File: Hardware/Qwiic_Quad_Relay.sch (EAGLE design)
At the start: 65 parts, among them J2 Qwiic Right Angle, J3 Qwiic Right Angle, J4 AVR_SPI_PROG_3X2TESTPOINTS, J9 POWER_JACK, K1 RELAY-SPDT-JZC-11F, K2 RELAY-SPDT-JZC-11F, K3 RELAY-SPDT-JZC-11F, K4 RELAY-SPDT-JZC-11F, Q1 600mA/40V, Q2 600mA/40V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

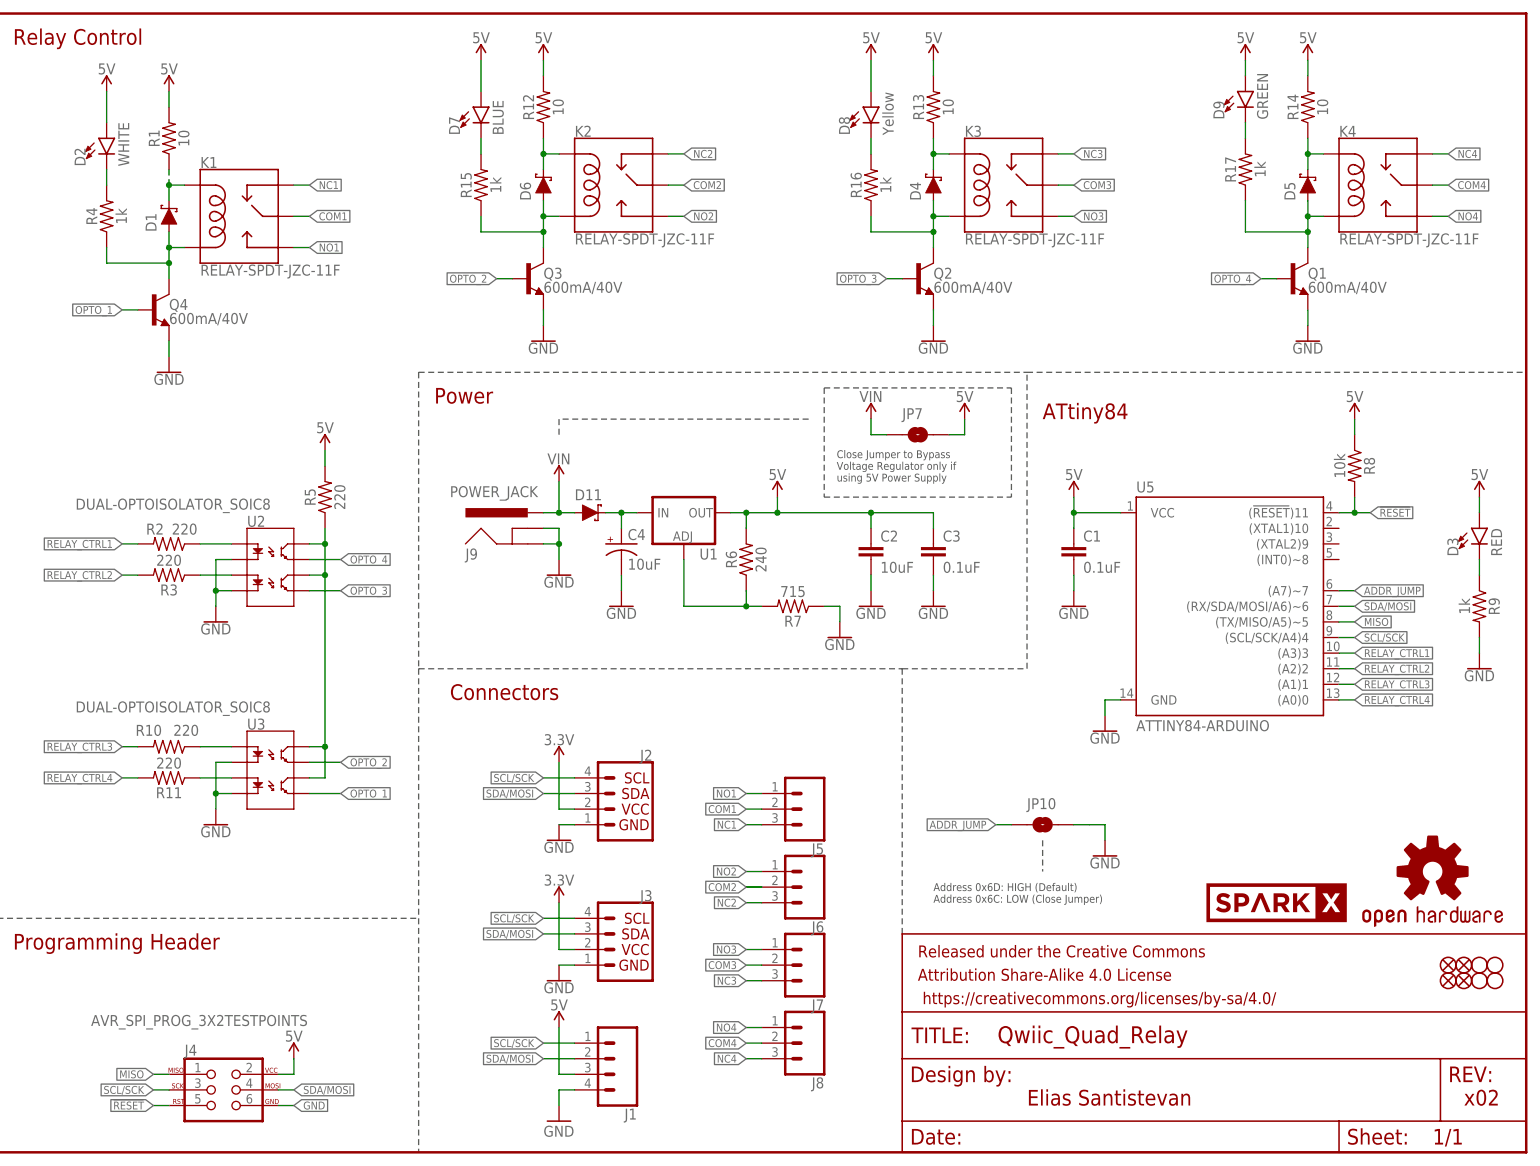
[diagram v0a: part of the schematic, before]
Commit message: Updated to v10 and updated example code that adds commented out line for second i2c address
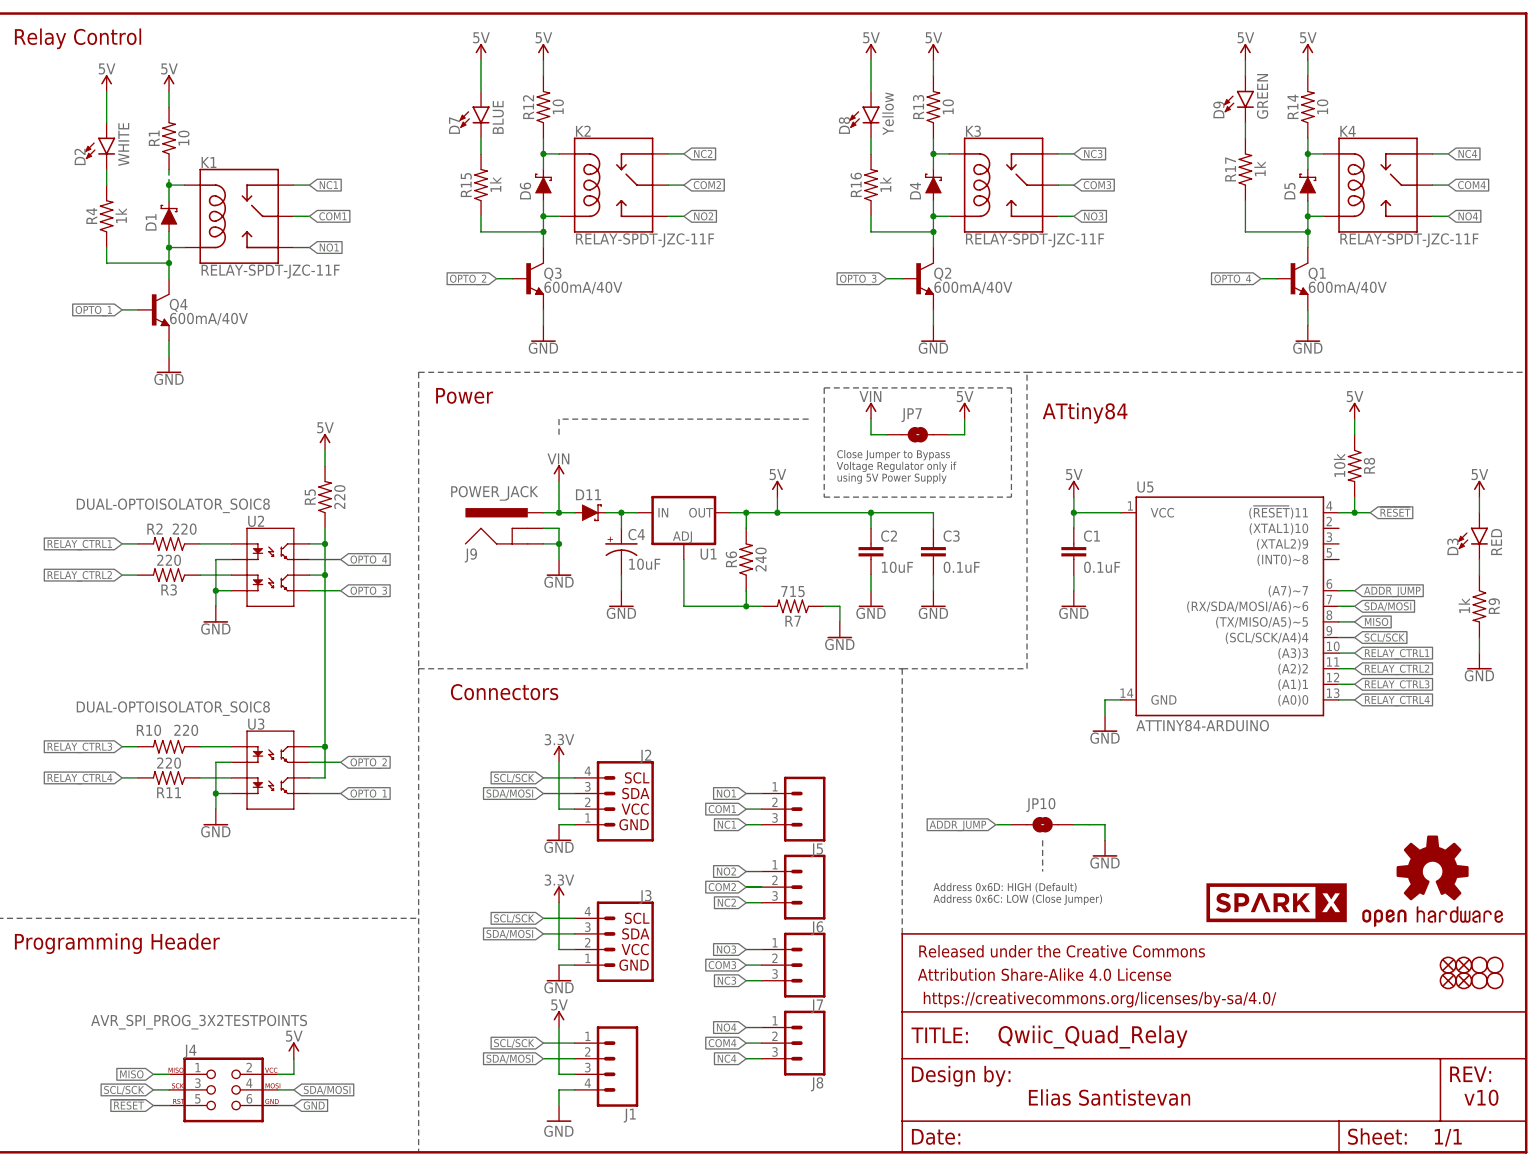
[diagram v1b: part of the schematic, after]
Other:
- note added: "v10"
- note removed: "x02"

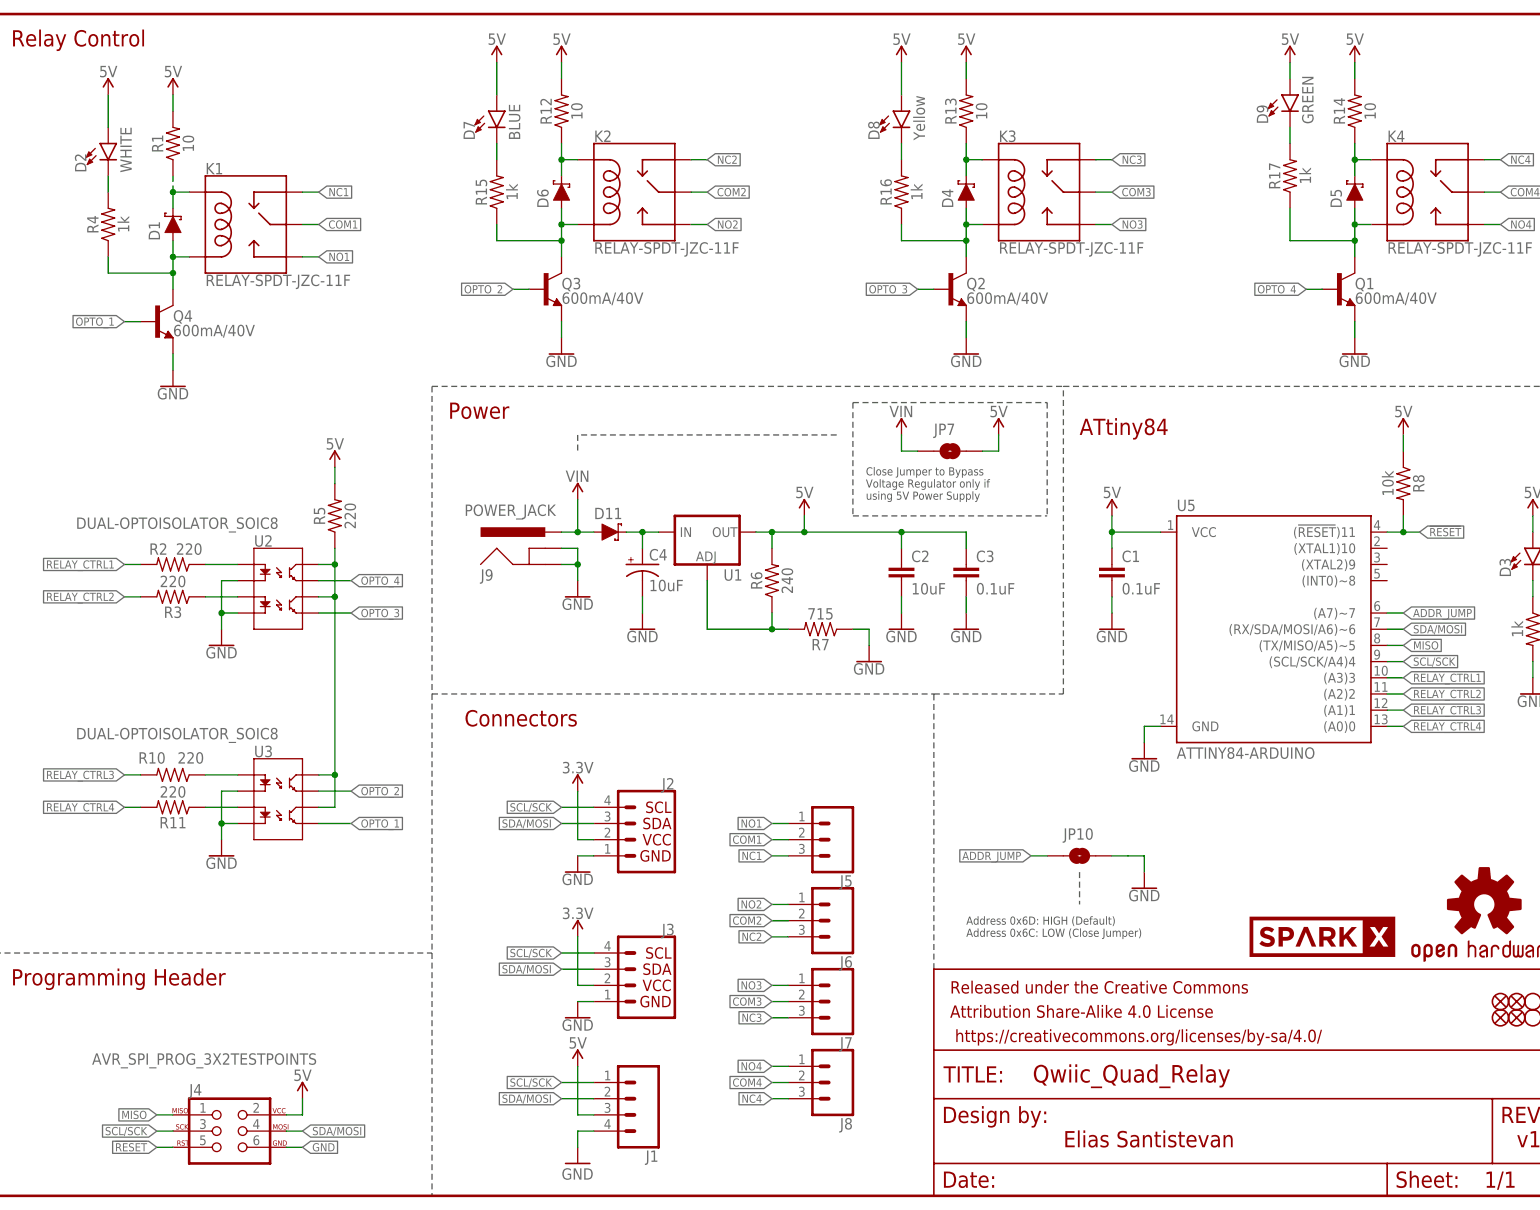
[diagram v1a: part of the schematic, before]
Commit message: Reduces current consumption on every relay channel, seperates 3.3V and 5V system
*Current consumption:
-10 Ohm coil resistor changed to 33 Ohm
-220 Ohm reistor into base of NPN changed to 330
*3.3V Qwiic System:
-Put ATtiny84 back onto the 3.3V Qwiic System
-Changed OptoIsolator resistors from 220 Ohm to 100 Ohm to hit current requirements
*Changed all LEDs to blue
*Changed SparkX labels to SparkFun labels
*Reduced relay trace width to 110 mils (from 160 -overkill)
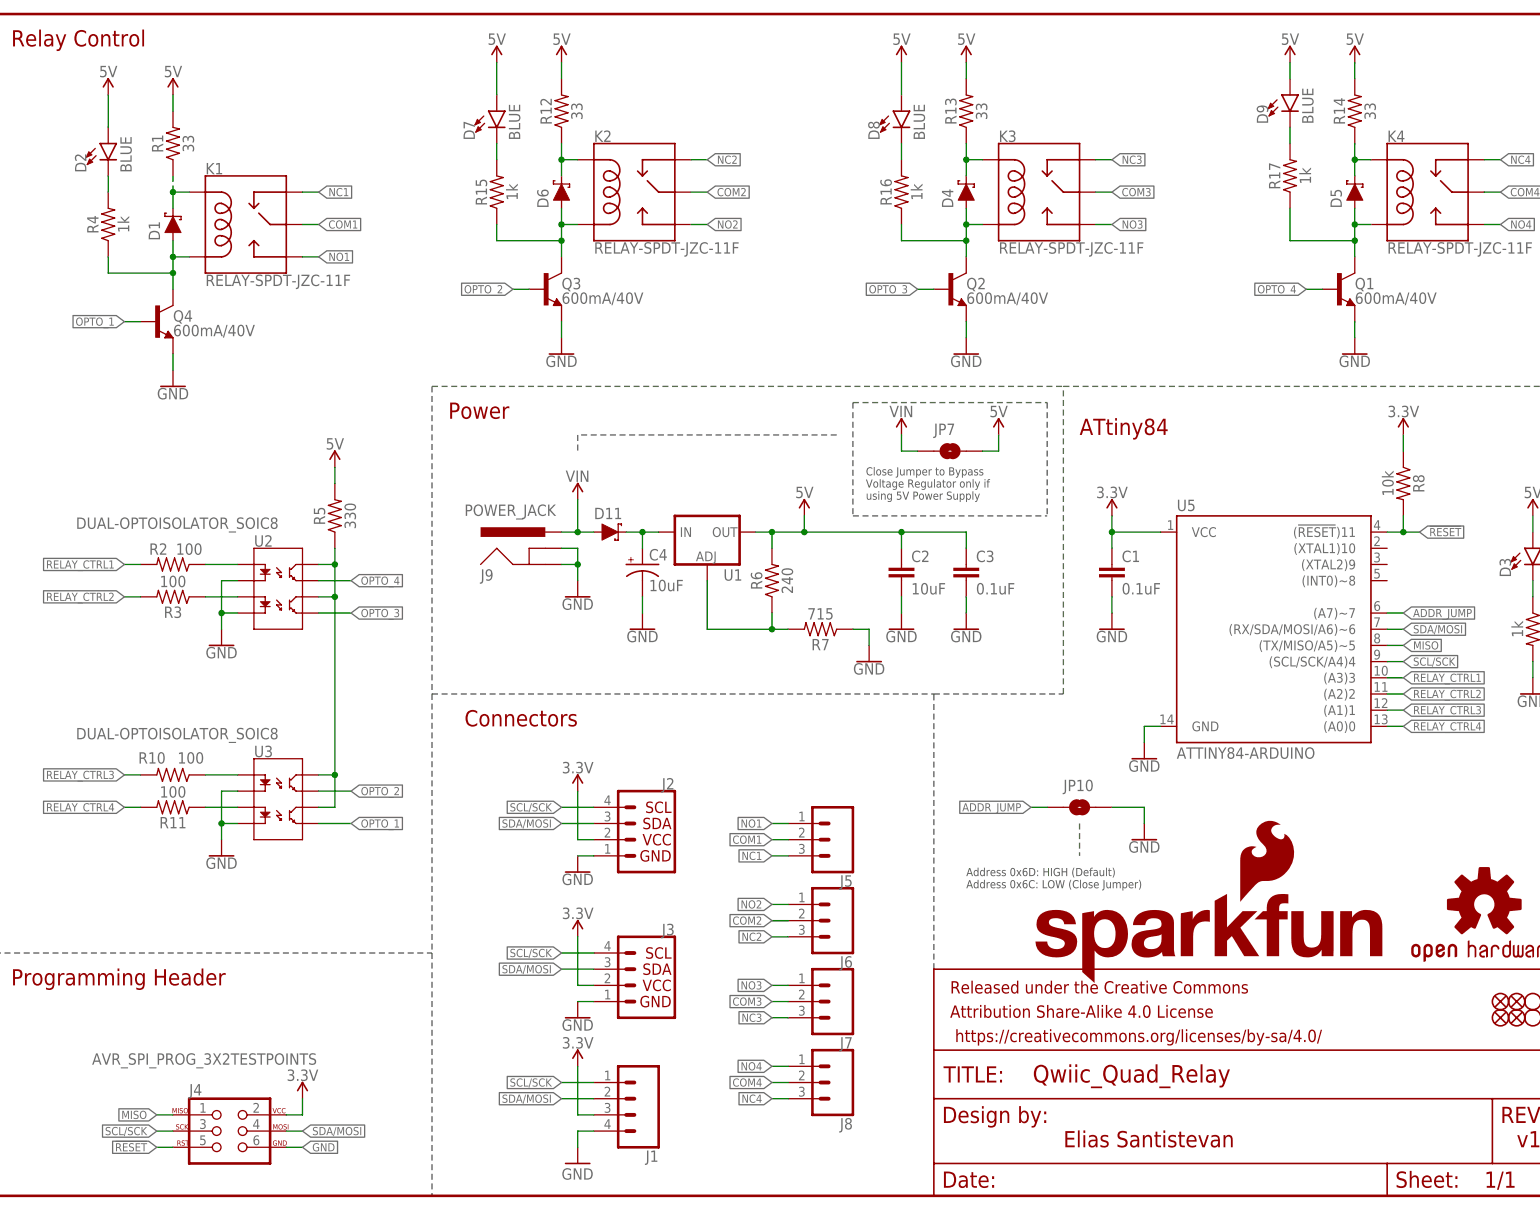
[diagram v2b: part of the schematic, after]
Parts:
- removed U$12: SPARKX-LOGO4, SparkX:SPARKX-LOGO4
- added LOGO2: SFE_LOGO_NAME_FLAME.1_INCH, SparkFun-Aesthetics:SFE_LOGO_NAME_FLAME.1_INCH
- D2: value WHITE -> BLUE; device SparkFun-LED:LED-WHITE0603 -> SparkFun-LED:LED-BLUE0603
- D8: value Yellow -> BLUE; device SparkFun-LED:LED-YELLOW0603 -> SparkFun-LED:LED-BLUE0603
- D9: value GREEN -> BLUE; device SparkFun-LED:LED-GREEN0603 -> SparkFun-LED:LED-BLUE0603
- R1, R12, R13, R14: value 10 -> 33; device SparkFun-Resistors:10OHM-0603-1/10W-5% -> SparkFun-Resistors:33OHM-0603-1/10W-1%
- R10, R11, R2, R3: value 220 -> 100; device SparkFun-Resistors:220OHM-0603-1/10W-1% -> SparkFun-Resistors:100OHM-0603-1/10W-1%
- R5: value 220 -> 330; device SparkFun-Resistors:220OHM-0603-1/10W-1% -> SparkFun-Resistors:330OHM-0603-1/10W-1%
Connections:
- net 3.3V: now also C1.1, J1.3, J4.2, R8.1, U5.VCC
- net 5V: no longer C1.1, J1.3, J4.2, R8.1, U5.VCC
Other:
- moved on the sheet: JP10

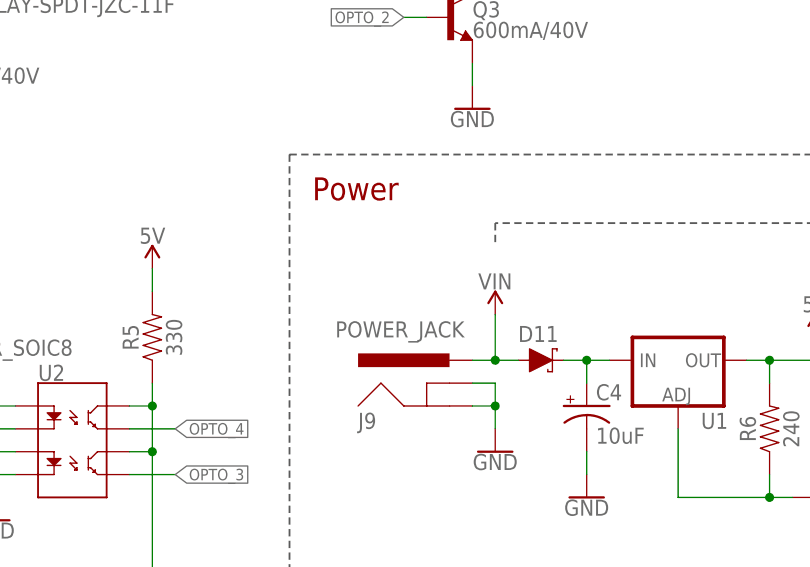
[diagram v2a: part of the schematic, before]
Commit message: Adds selective soldering path to documents layer
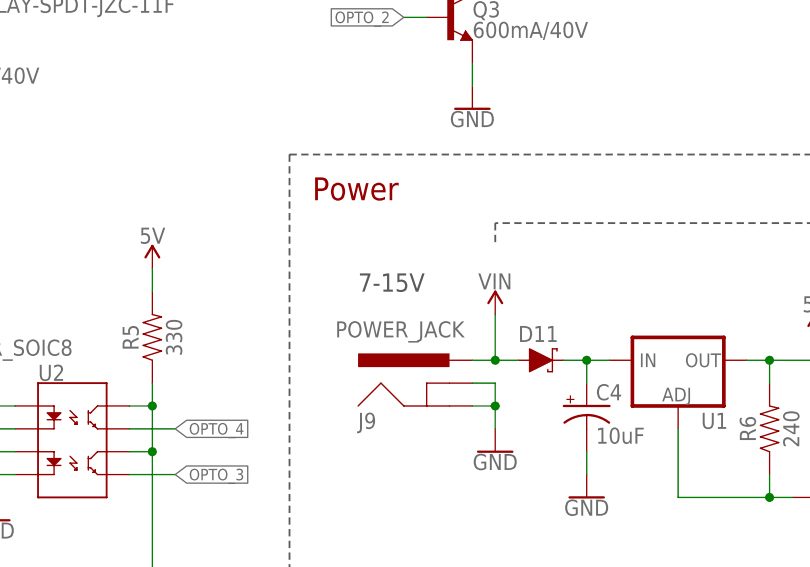
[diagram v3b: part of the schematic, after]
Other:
- note added: "7-15V"
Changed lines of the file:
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@@
 Address 0x6C: LOW (Close Jumper)</text>
 <wire x1="170.18" y1="58.42" x2="170.18" y2="53.34" width="0.2032" layer="97" style="dashdot"/>
+<text x="76.2" y="111.76" size="2.032" layer="97" font="vector">7-15V</text>
 </plain>
 <instances>

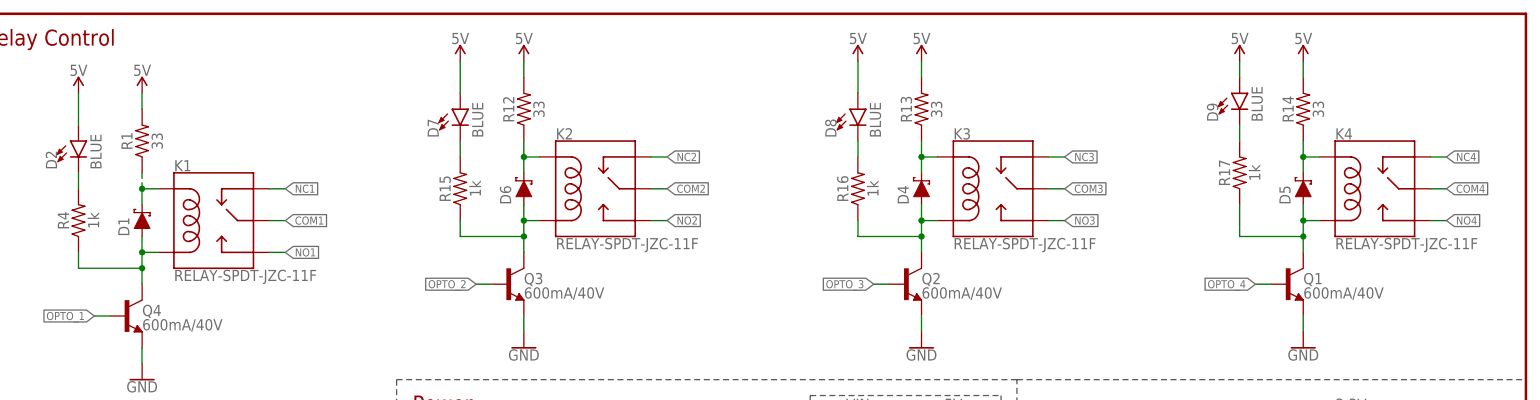
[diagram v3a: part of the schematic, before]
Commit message: Moves 33 Ohm resistor to after the coil so that drop doesn't occur before it.
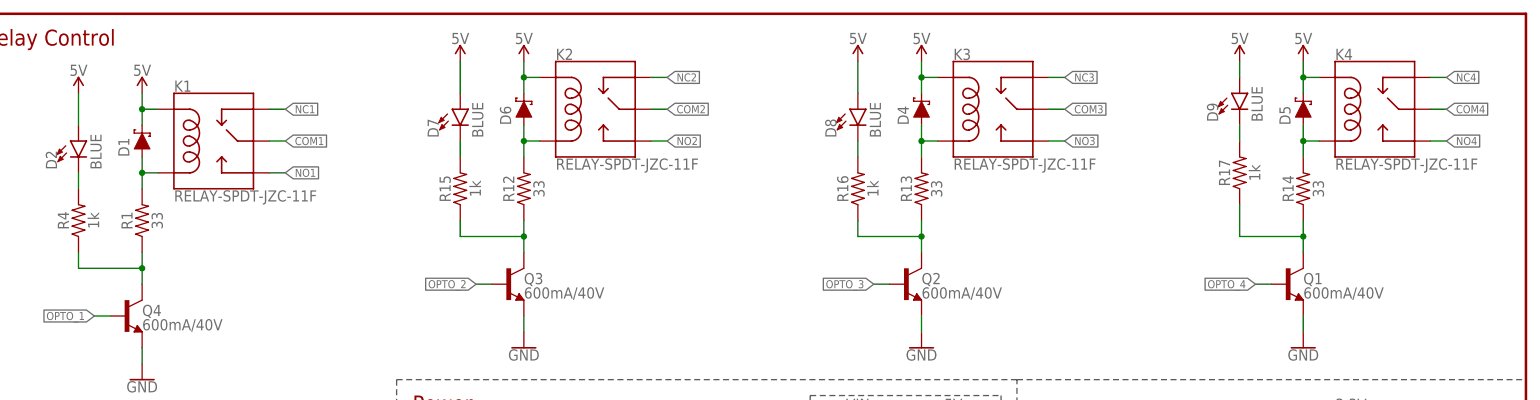
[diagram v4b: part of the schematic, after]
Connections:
- removed net N$1: D6.C, K2.COIL1, R12.1
- removed net N$14: D4.C, K3.COIL1, R13.1
- removed net N$16: D5.C, K4.COIL1, R14.1
- removed net N$7: D1.C, K1.COIL1, R1.1
- new net N$10: D1.A, K1.COIL2, R1.2
- new net N$18: D6.A, K2.COIL2, R12.2
- new net N$23: D4.A, K3.COIL2, R13.2
- new net N$24: D5.A, K4.COIL2, R14.2
- net 5V: now also D1.C, D4.C, D5.C, D6.C, K1.COIL1, K2.COIL1, K3.COIL1, K4.COIL1; no longer R1.2, R12.2, R13.2, R14.2
- net N$12: now also R12.1; no longer D6.A, K2.COIL2
- net N$15: now also R13.1; no longer D4.A, K3.COIL2
- net N$17: now also R14.1; no longer D5.A, K4.COIL2
- net N$2: now also R1.1; no longer D1.A, K1.COIL2
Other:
- moved on the sheet: D1, D4, D5, D6, K1, K2, K3, K4, R1, R12, R13, R14
